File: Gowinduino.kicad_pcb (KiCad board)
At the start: 2 copper layers, 68.6 x 53.3 mm, 13 parts, among them J1 Power, J2 Analog, J3 Digital, J4 Digital, J5 SPI, U1 GW1NSR-4CQN48P, U2 W25Q32JVSS

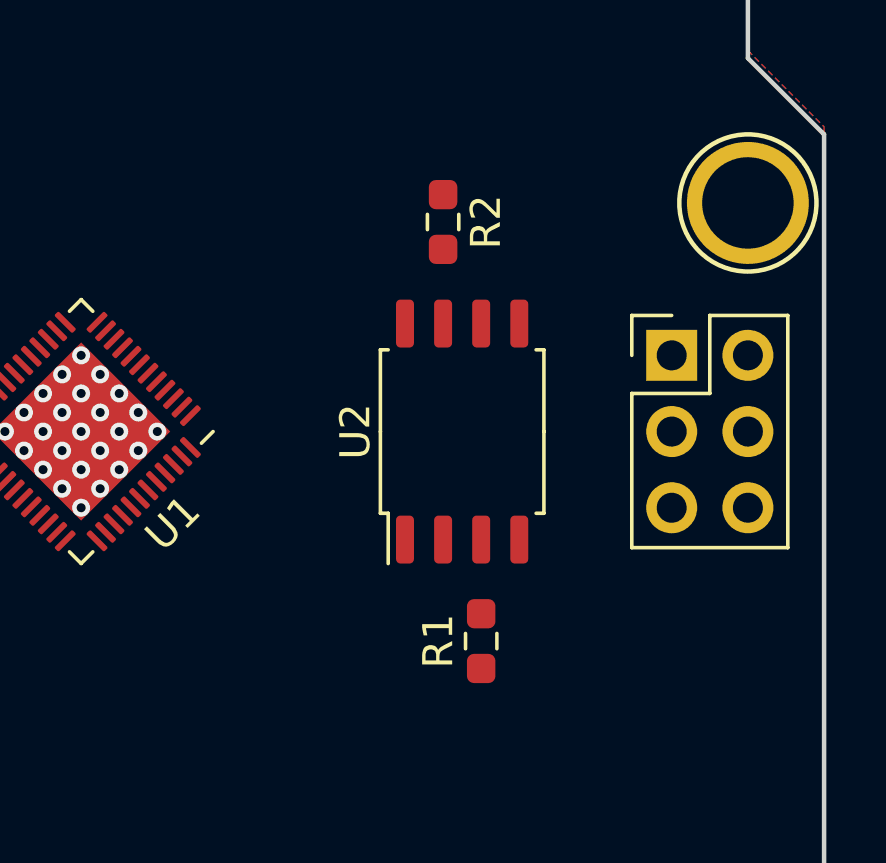
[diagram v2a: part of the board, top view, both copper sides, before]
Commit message: PCB: Locating SPI Flash resistors.
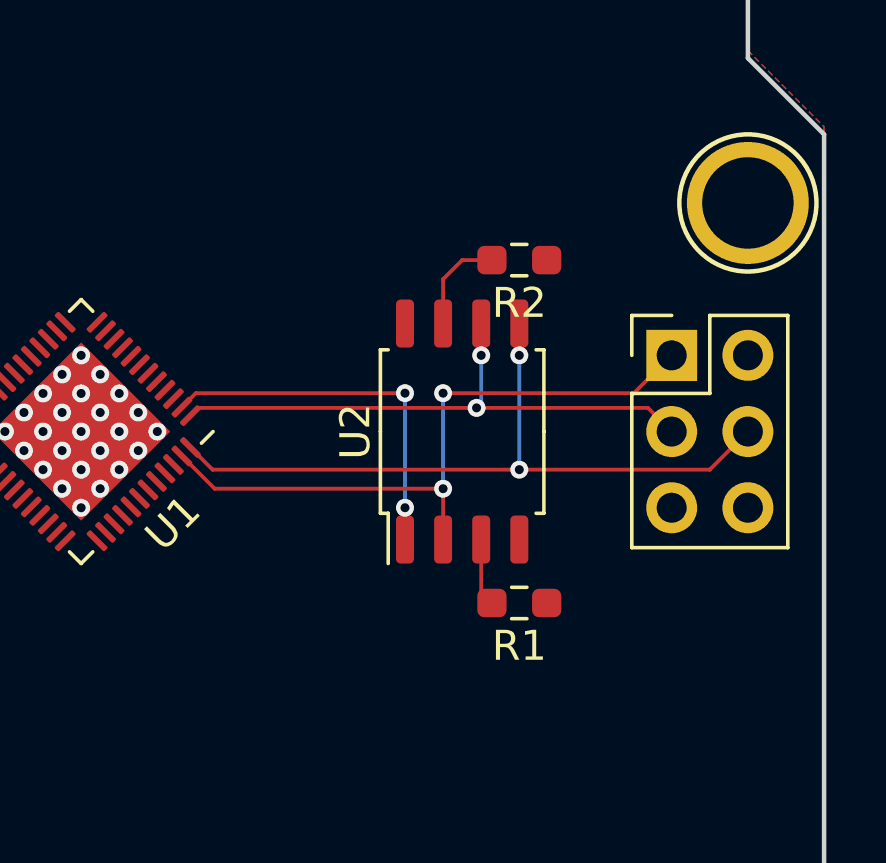
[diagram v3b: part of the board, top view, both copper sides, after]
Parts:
- moved R2 2.84 mm to (169.4, 92.7), turned to 180 degrees
- moved R1 1.80 mm to (169.4, 104.1), turned to 180 degrees
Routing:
- net /MOSI: track 0.00 -> 24.3 mm, vias 0 -> 2
- net /MISO: track 0.00 -> 22.2 mm, vias 0 -> 2
- net /SCLK: track 0.00 -> 19.4 mm, vias 0 -> 2
- net /~CS: track 0.00 -> 12.5 mm, vias 0 -> 2
- net Net-(R2-Pad2): track 0.00 -> 3.37 mm
- net Net-(R1-Pad2): track 0.00 -> 2.26 mm
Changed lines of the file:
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@@
     (thickness 1.6)
     (drawings 26)
-    (tracks 25)
+    (tracks 61)
     (zones 0)
     (modules 13)
@@
   )
   (module Resistor_SMD:R_0603_1608Metric_Pad0.98x0.95mm_HandSolder (layer F.Cu)
-    (at 166.878 91.44 270)
+    (at 169.418 92.71 180)
     (descr "Resistor SMD 0603 (1608 Metric), square (rectangular) end terminal, IPC_7351 nominal with elongated pad for handsoldering. (Body size source: IPC-SM-782 page 72, https://www.pcb-3d.com/wordpress/wp-content/uploads/ipc-sm-782a_amendment_1_and_2.pdf), generated with kicad-footprint-generator")
     (tags "resistor handsolder")
     (attr smd)
-    (fp_text reference R2 (at 0 -1.43 90) (layer F.SilkS)
-      (effects (font (size 1 1) (thickness 0.15)))
-    )
-    (fp_text value 10k (at 0 1.43 90) (layer F.Fab)
-      (effects (font (size 1 1) (thickness 0.15)))
-    )
-    (fp_text user %R (at 0 0 90) (layer F.Fab)
+    (fp_text reference R2 (at 0 -1.43) (layer F.SilkS)
+      (effects (font (size 1 1) (thickness 0.15)))
+    )
+    (fp_text value 10k (at 0 1.43) (layer F.Fab)
+      (effects (font (size 1 1) (thickness 0.15)))
+    )
+    (fp_text user %R (at 0 0) (layer F.Fab)
       (effects (font (size 0.4 0.4) (thickness 0.06)))
     )
@@
     (fp_line (start 1.65 -0.73) (end 1.65 0.73) (layer F.CrtYd) (width 0.05))
     (fp_line (start 1.65 0.73) (end -1.65 0.73) (layer F.CrtYd) (width 0.05))
-    (pad 2 smd roundrect (at 0.9125 0 270) (size 0.975 0.95) (layers F.Cu F.Paste F.Mask) (roundrect_rratio 0.25)
+    (pad 2 smd roundrect (at 0.9125 0 180) (size 0.975 0.95) (layers F.Cu F.Paste F.Mask) (roundrect_rratio 0.25)
       (net 9 "Net-(R2-Pad2)"))
-    (pad 1 smd roundrect (at -0.9125 0 270) (size 0.975 0.95) (layers F.Cu F.Paste F.Mask) (roundrect_rratio 0.25)
+    (pad 1 smd roundrect (at -0.9125 0 180) (size 0.975 0.95) (layers F.Cu F.Paste F.Mask) (roundrect_rratio 0.25)
       (net 3 +3V3))
     (model ${KISYS3DMOD}/Resistor_SMD.3dshapes/R_0603_1608Metric.wrl
@@
   )
   (module Resistor_SMD:R_0603_1608Metric_Pad0.98x0.95mm_HandSolder (layer F.Cu)
-    (at 168.148 105.41 90)
+    (at 169.418 104.14 180)
     (descr "Resistor SMD 0603 (1608 Metric), square (rectangular) end terminal, IPC_7351 nominal with elongated pad for handsoldering. (Body size source: IPC-SM-782 page 72, https://www.pcb-3d.com/wordpress/wp-content/uploads/ipc-sm-782a_amendment_1_and_2.pdf), generated with kicad-footprint-generator")
     (tags "resistor handsolder")
     (attr smd)
-    (fp_text reference R1 (at 0 -1.43 90) (layer F.SilkS)
-      (effects (font (size 1 1) (thickness 0.15)))
-    )
-    (fp_text value 10k (at 0 1.43 90) (layer F.Fab)
-      (effects (font (size 1 1) (thickness 0.15)))
-    )
-    (fp_text user %R (at 0 0 90) (layer F.Fab)
+    (fp_text reference R1 (at 0 -1.43) (layer F.SilkS)
+      (effects (font (size 1 1) (thickness 0.15)))
+    )
+    (fp_text value 10k (at 0 1.43) (layer F.Fab)
+      (effects (font (size 1 1) (thickness 0.15)))
+    )
+    (fp_text user %R (at 0 0) (layer F.Fab)
       (effects (font (size 0.4 0.4) (thickness 0.06)))
     )
@@
     (fp_line (start 1.65 -0.73) (end 1.65 0.73) (layer F.CrtYd) (width 0.05))
     (fp_line (start 1.65 0.73) (end -1.65 0.73) (layer F.CrtYd) (width 0.05))
-    (pad 2 smd roundrect (at 0.9125 0 90) (size 0.975 0.95) (layers F.Cu F.Paste F.Mask) (roundrect_rratio 0.25)
+    (pad 2 smd roundrect (at 0.9125 0 180) (size 0.975 0.95) (layers F.Cu F.Paste F.Mask) (roundrect_rratio 0.25)
       (net 8 "Net-(R1-Pad2)"))
-    (pad 1 smd roundrect (at -0.9125 0 90) (size 0.975 0.95) (layers F.Cu F.Paste F.Mask) (roundrect_rratio 0.25)
+    (pad 1 smd roundrect (at -0.9125 0 180) (size 0.975 0.95) (layers F.Cu F.Paste F.Mask) (roundrect_rratio 0.25)
       (net 3 +3V3))
     (model ${KISYS3DMOD}/Resistor_SMD.3dshapes/R_0603_1608Metric.wrl
@@
   (via (at 154.178 97.79) (size 0.6) (drill 0.3) (layers F.Cu B.Cu) (net 2))
   (via (at 154.813 98.425) (size 0.6) (drill 0.3) (layers F.Cu B.Cu) (net 2))
+  (segment (start 158.4546 98.95533) (end 159.19427 99.695) (width 0.127) (layer F.Cu) (net 5))
+  (segment (start 175.768 99.695) (end 177.038 98.425) (width 0.127) (layer F.Cu) (net 5))
+  (via (at 169.418 95.885) (size 0.6) (drill 0.3) (layers F.Cu B.Cu) (net 5))
+  (segment (start 169.418 94.825) (end 169.418 95.885) (width 0.127) (layer F.Cu) (net 5))
+  (segment (start 169.418 95.885) (end 169.418 99.695) (width 0.127) (layer B.Cu) (net 5))
+  (via (at 169.418 99.695) (size 0.6) (drill 0.3) (layers F.Cu B.Cu) (net 5))
+  (segment (start 169.418 99.695) (end 175.768 99.695) (width 0.127) (layer F.Cu) (net 5))
+  (segment (start 159.19427 99.695) (end 169.418 99.695) (width 0.127) (layer F.Cu) (net 5))
+  (segment (start 173.709483 97.636483) (end 174.498 98.425) (width 0.127) (layer F.Cu) (net 6))
+  (segment (start 158.4546 97.89467) (end 158.712787 97.636483) (width 0.127) (layer F.Cu) (net 6))
+  (via (at 168.148 95.885) (size 0.6) (drill 0.3) (layers F.Cu B.Cu) (net 6))
+  (segment (start 168.148 94.825) (end 168.148 95.885) (width 0.127) (layer F.Cu) (net 6))
+  (segment (start 168.148 97.482966) (end 167.994483 97.636483) (width 0.127) (layer B.Cu) (net 6))
+  (via (at 167.994483 97.636483) (size 0.6) (drill 0.3) (layers F.Cu B.Cu) (net 6))
+  (segment (start 168.148 95.885) (end 168.148 97.482966) (width 0.127) (layer B.Cu) (net 6))
+  (segment (start 167.994483 97.636483) (end 173.709483 97.636483) (width 0.127) (layer F.Cu) (net 6))
+  (segment (start 158.712787 97.636483) (end 167.994483 97.636483) (width 0.127) (layer F.Cu) (net 6))
+  (via (at 166.878 100.33) (size 0.6) (drill 0.3) (layers F.Cu B.Cu) (net 7))
+  (segment (start 159.263584 100.33) (end 166.878 100.33) (width 0.127) (layer F.Cu) (net 7))
+  (segment (start 158.171757 99.238173) (end 159.263584 100.33) (width 0.127) (layer F.Cu) (net 7))
+  (segment (start 166.878 102.025) (end 166.878 100.33) (width 0.127) (layer F.Cu) (net 7))
+  (via (at 166.878 97.145983) (size 0.6) (drill 0.3) (layers F.Cu B.Cu) (net 7))
+  (segment (start 166.878 97.145983) (end 166.878 100.33) (width 0.127) (layer B.Cu) (net 7))
+  (segment (start 173.237017 97.145983) (end 174.498 95.885) (width 0.127) (layer F.Cu) (net 7))
+  (segment (start 166.878 97.145983) (end 173.237017 97.145983) (width 0.127) (layer F.Cu) (net 7))
+  (segment (start 168.148 103.7825) (end 168.5055 104.14) (width 0.127) (layer F.Cu) (net 8))
+  (segment (start 168.148 102.025) (end 168.148 103.7825) (width 0.127) (layer F.Cu) (net 8))
+  (segment (start 166.878 94.825) (end 166.878 93.345) (width 0.127) (layer F.Cu) (net 9))
+  (segment (start 167.513 92.71) (end 168.5055 92.71) (width 0.127) (layer F.Cu) (net 9))
+  (segment (start 166.878 93.345) (end 167.513 92.71) (width 0.127) (layer F.Cu) (net 9))
+  (via (at 165.608 97.145983) (size 0.6) (drill 0.3) (layers F.Cu B.Cu) (net 12))
+  (segment (start 158.637601 97.145983) (end 165.608 97.145983) (width 0.127) (layer F.Cu) (net 12))
+  (segment (start 158.171757 97.611827) (end 158.637601 97.145983) (width 0.127) (layer F.Cu) (net 12))
+  (segment (start 165.608 100.965) (end 165.608 102.025) (width 0.127) (layer F.Cu) (net 12))
+  (segment (start 165.608 97.145983) (end 165.608 100.965) (width 0.127) (layer B.Cu) (net 12))
+  (via (at 165.608 100.965) (size 0.6) (drill 0.3) (layers F.Cu B.Cu) (net 12))
   (zone (net 2) (net_name GND) (layer F.Cu) (hatch edge 0.508)
     (connect_pads (clearance 0.1905))

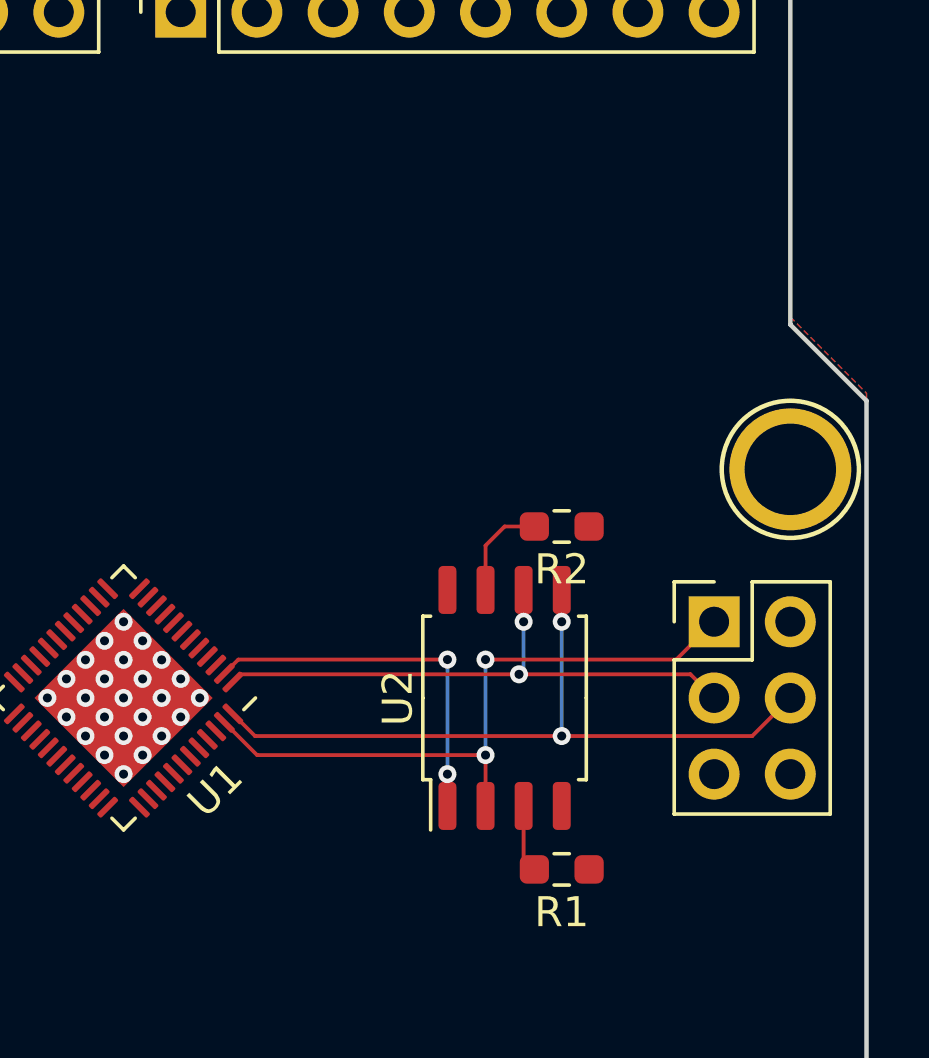
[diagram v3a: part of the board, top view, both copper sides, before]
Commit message: PCB: Hooking up the JTAG port.
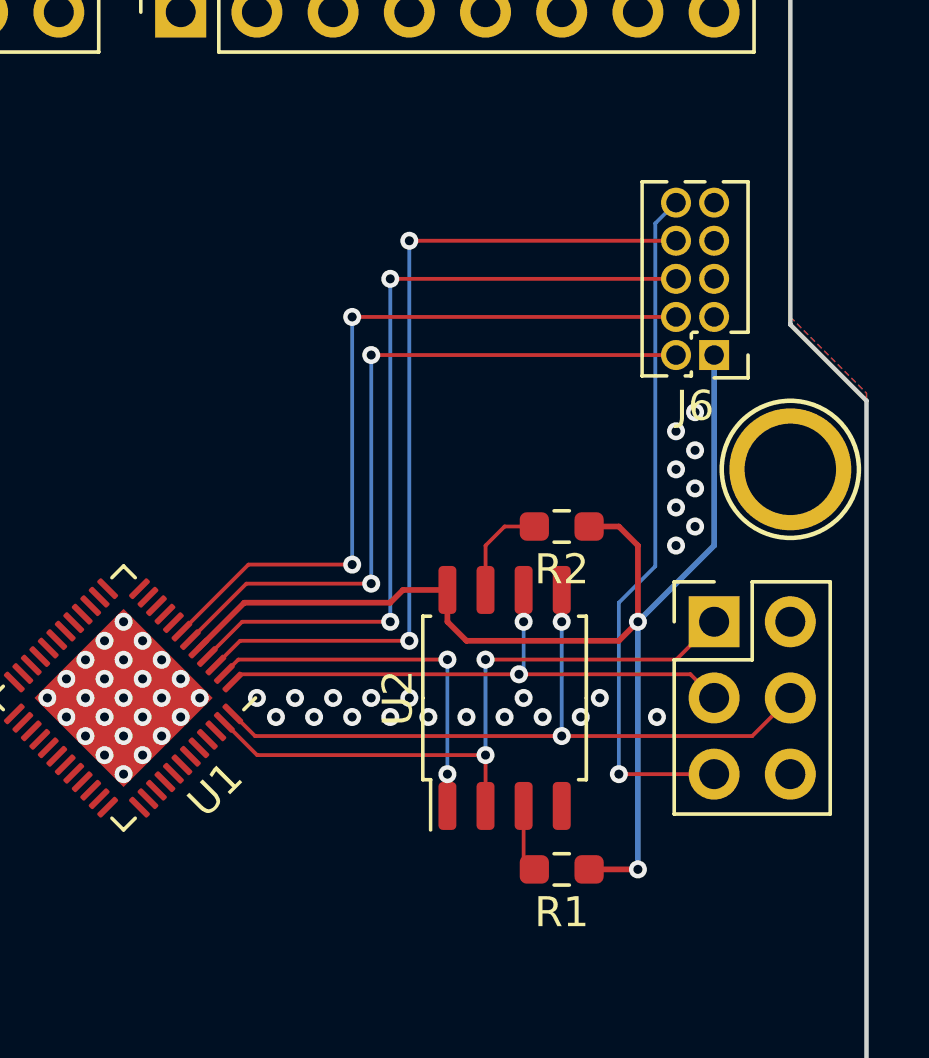
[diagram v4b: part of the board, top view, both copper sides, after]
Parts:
- added J6: JTAG, Connector_PinHeader_1.27mm:PinHeader_2x05_P1.27mm_Vertical, F.Cu at (174.5, 87.0)
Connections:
- U1 pad 3: (no net) -> /TDI
- U1 pad 4: (no net) -> /TDO
- U1 pad 6: (no net) -> /TMS
- U1 pad 7: (no net) -> /TCK
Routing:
- net +3V3: track 0.00 -> 41.3 mm, vias 0 -> 2
- net /TDI: track 0.00 -> 29.0 mm, vias 0 -> 2
- net /TDO: track 0.00 -> 27.5 mm, vias 0 -> 2
- net /TCK: track 0.00 -> 25.6 mm, vias 0 -> 2
- net /TMS: track 0.00 -> 24.6 mm, vias 0 -> 2
- net /~RESET: track 0.00 -> 23.0 mm, vias 0 -> 1
- net GND: vias 25 -> 50

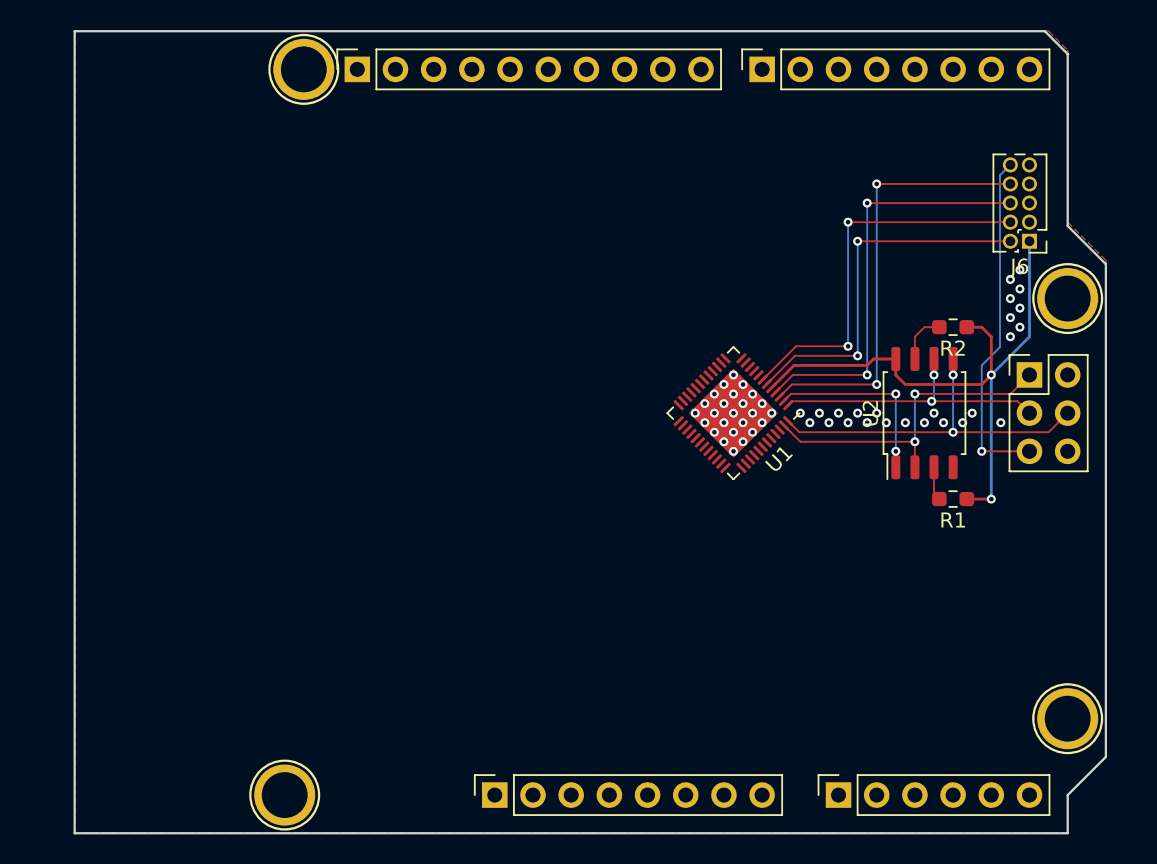
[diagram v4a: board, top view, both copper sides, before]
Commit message: PCB: Hookup all 3.3V IO pins
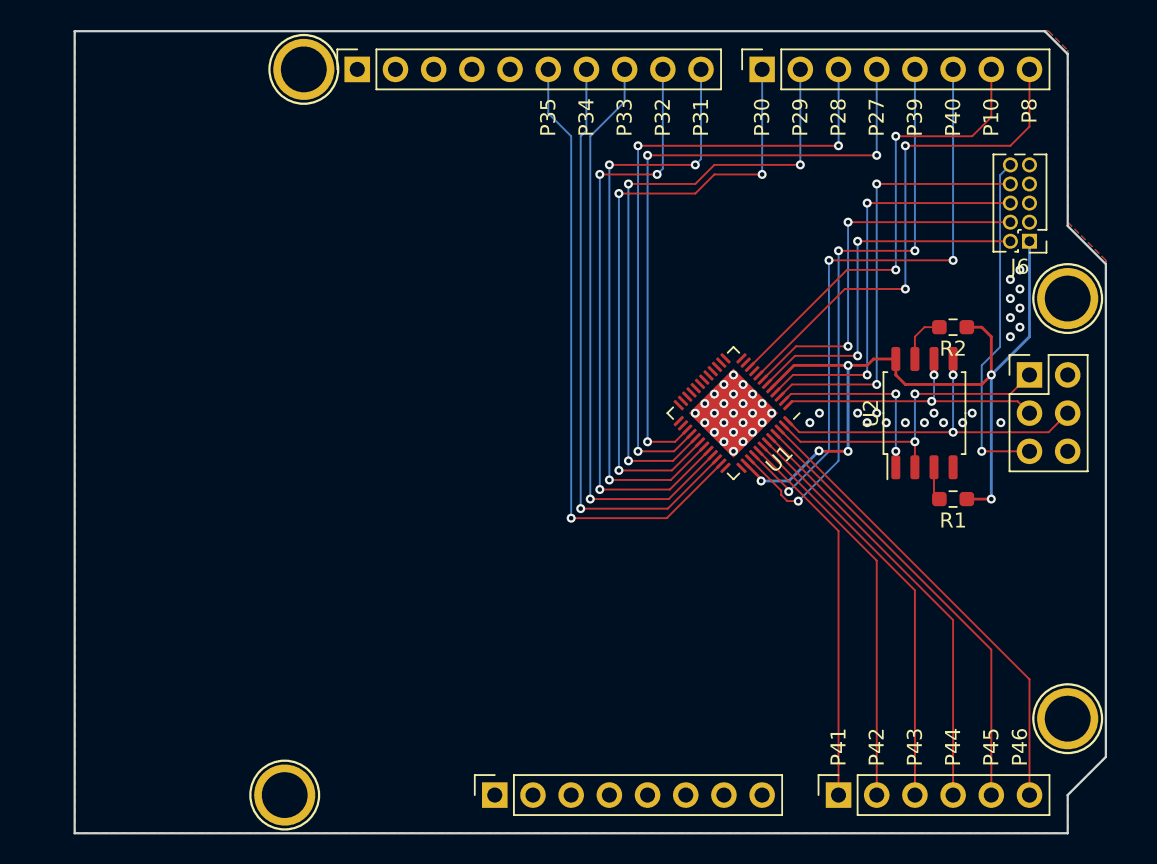
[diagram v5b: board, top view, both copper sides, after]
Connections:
- J2 pad 1: (no net) -> /A0
- J2 pad 2: (no net) -> /A1
- J2 pad 3: (no net) -> /A2
- J2 pad 4: (no net) -> /A3
- J2 pad 5: (no net) -> /A4
- J2 pad 6: (no net) -> /A5
- J3 pad 10: (no net) -> /8
- J3 pad 6: (no net) -> /12
- J3 pad 7: (no net) -> /11
- J3 pad 8: (no net) -> /10
- J3 pad 9: (no net) -> /9
- J4 pad 1: (no net) -> /7
- J4 pad 2: (no net) -> /6
- J4 pad 3: (no net) -> /5
- J4 pad 4: (no net) -> /4
- J4 pad 5: (no net) -> /3
- J4 pad 6: (no net) -> /2
- J4 pad 7: (no net) -> /1
- J4 pad 8: (no net) -> /0
- U1 pad 10: (no net) -> /1
- U1 pad 27: (no net) -> /4
- U1 pad 28: (no net) -> /5
- U1 pad 29: (no net) -> /6
- U1 pad 30: (no net) -> /7
- U1 pad 31: (no net) -> /8
- U1 pad 32: (no net) -> /9
- U1 pad 33: (no net) -> /10
- U1 pad 34: (no net) -> /11
- U1 pad 35: (no net) -> /12
- U1 pad 39: (no net) -> /3
- U1 pad 40: (no net) -> /2
- U1 pad 41: (no net) -> /A0
- U1 pad 42: (no net) -> /A1
- U1 pad 43: (no net) -> /A2
- U1 pad 44: (no net) -> /A3
- U1 pad 45: (no net) -> /A4
- U1 pad 46: (no net) -> /A5
- U1 pad 8: (no net) -> /0
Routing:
- net /4: track 0.00 -> 43.0 mm, vias 0 -> 3
- net /5: track 0.00 -> 42.8 mm, vias 0 -> 3
- net /12: track 0.00 -> 42.0 mm, vias 0 -> 1
- net /6: track 0.00 -> 41.8 mm, vias 0 -> 3
- net /7: track 0.00 -> 41.6 mm, vias 0 -> 3
- net /2: track 0.00 -> 40.8 mm, vias 0 -> 3
- net /8: track 0.00 -> 40.4 mm, vias 0 -> 3
- net /9: track 0.00 -> 40.2 mm, vias 0 -> 3
- net /11: track 0.00 -> 39.8 mm, vias 0 -> 1
- net /3: track 0.00 -> 39.4 mm, vias 0 -> 3
- net /10: track 0.00 -> 38.9 mm, vias 0 -> 1
- net /0: track 0.00 -> 34.3 mm, vias 0 -> 2
- net /1: track 0.00 -> 31.3 mm, vias 0 -> 2
- net /A5: track 0.00 -> 31.2 mm
- net /A4: track 0.00 -> 30.0 mm
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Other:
- board text added: "P10"
- board text added: "P27"
- board text added: "P28"
- board text added: "P29"
- board text added: "P30"
- board text added: "P31"
- board text added: "P32"
- board text added: "P33"
- board text added: "P34"
- board text added: "P35"
- board text added: "P39"
- board text added: "P40"
- board text added: "P41"
- board text added: "P42"
- board text added: "P43"
- board text added: "P44"
- board text added: "P45"
- board text added: "P46"
- board text added: "P8"
